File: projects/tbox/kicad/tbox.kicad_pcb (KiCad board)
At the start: 4 copper layers, 300 x 270 mm, 355 parts, among them J1001 PHONES A 3.5, J1002 PHONES A 1/4, J1003 PHONES B 3.5, J1004 PHONES B 1/4, J1005 TO CTRL J2001, J1101 MIC 3.5, J1102 MIC 1/4, J1103 HEADSET, J1104 SPARE, J1301 MIC 3.5, J1302 MIC 1/4, J1303 HEADSET, J1304 SPARE, J2001 TO FRONT J1005, J2002 TO REAR J3001, J3001 TO CTRL J2002, J3101 PWR IN (panel Powerpole), J3201 PTT A 3.5, J3202 PTT A 1/4, J3203 PTT B 3.5, J3204 PTT B 1/4, J3205 CW SPARE, J3206 RIG DE-9, J3301 LINE L SRC, J3302 LINE R SRC, J3303 LINE OUT, Q2101 2N7002, Q2102 2N7002, Q2103 2N7002, Q2104 2N7002, Q2105 2N7002, Q2106 2N7002, Q2107 2N7002, Q2201 MMBT3904, Q2202 2N7002, Q3201 2N7002, SW2101 PTT A, SW2102 PTT B, SW2103 OVERRIDE, SW2104 MUTE A, SW2105 MUTE B, SW2201 INTERCOM, SW3201 GAIN A HI, SW3202 GAIN B HI, SW3203 BIAS A, SW3204 BIAS B, T3301 600R:600R, T3302 600R:600R, U1101 OPA1678, U1102 TS12A12511, U1201 TS12A12511, U1301 OPA1678, U1302 TS12A12511, U1401 TS12A12511, U2201 OPA1678, U2301 TS12A12511, U2401 NJM4556A, U2402 OPA1678, U2403 NJM4556A, U3101 ADP7142AUJZ-5.0, U3102 OPA1678, U3103 TPS7A4701, U3301 OPA1678, U3302 OPA1678, U3401 OPA1678

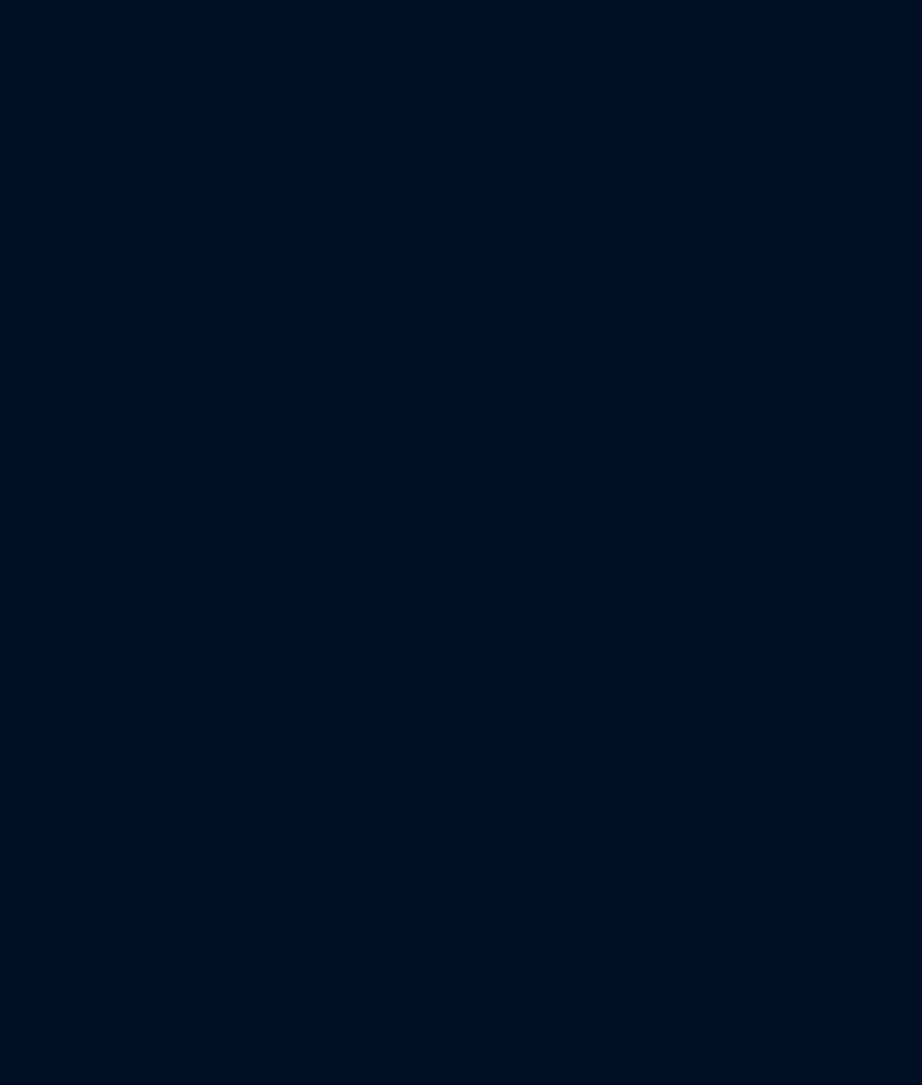
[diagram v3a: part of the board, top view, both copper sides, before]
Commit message: Footprints re-linked after the supply move (Update PCB from Schematic)
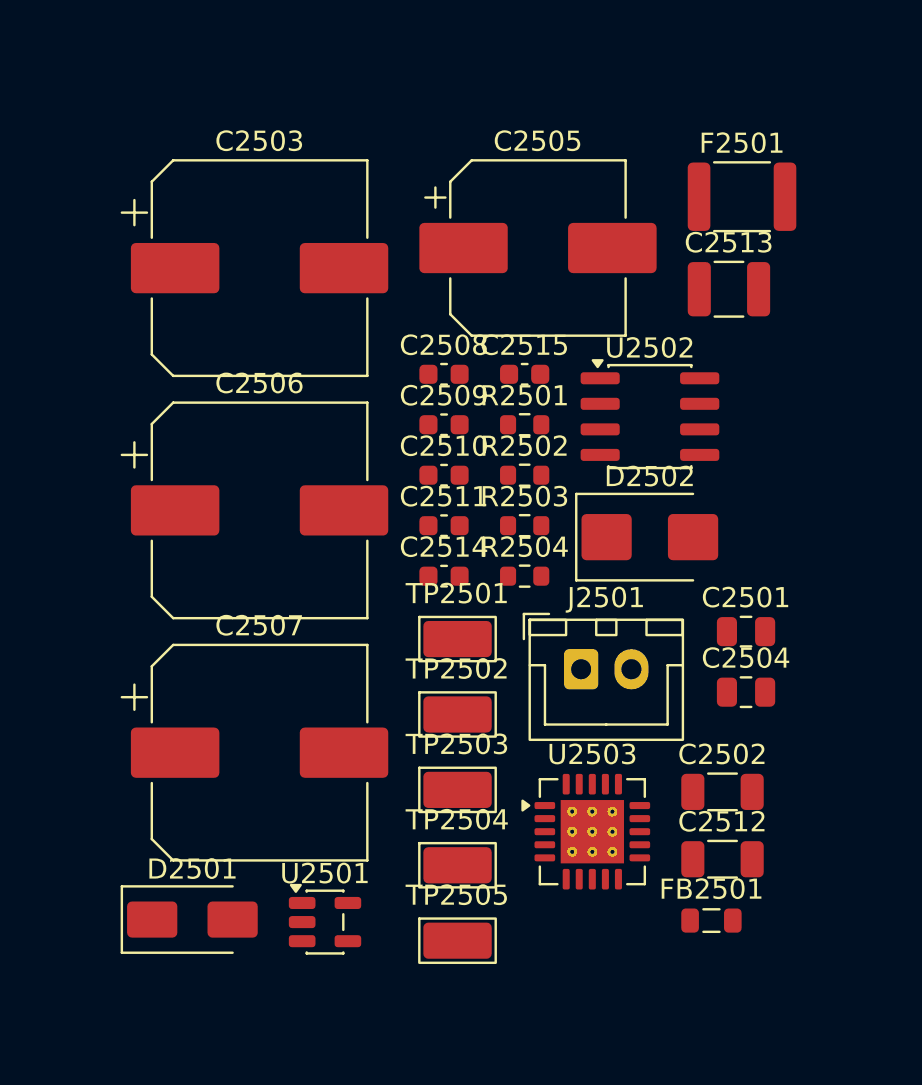
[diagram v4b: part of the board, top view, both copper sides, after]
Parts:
- added C2501: 4u7, Capacitor_SMD:C_0805_2012Metric, F.Cu at (94.6, 154.9)
- added C2502: 10u, Capacitor_SMD:C_1206_3216Metric, F.Cu at (93.4, 162.8)
- added C2503: 220u 35V, Capacitor_SMD:CP_Elec_10x10.5, F.Cu at (70.4, 136.8)
- added C2504: 4u7, Capacitor_SMD:C_0805_2012Metric, F.Cu at (94.6, 157.9)
- added C2505: 220u, Capacitor_SMD:CP_Elec_8x10.5, F.Cu at (84.3, 135.8)
- added C2506: 220u 35V, Capacitor_SMD:CP_Elec_10x10.5, F.Cu at (70.4, 148.8)
- added C2507: 470u, Capacitor_SMD:CP_Elec_10x10.5, F.Cu at (70.4, 160.9)
- added C2508: 100n, Capacitor_SMD:C_0603_1608Metric, F.Cu at (79.6, 142.1)
- added C2509: 100n, Capacitor_SMD:C_0603_1608Metric, F.Cu at (79.6, 144.6)
- added C2510: 1n, Capacitor_SMD:C_0603_1608Metric, F.Cu at (79.6, 147.1)
- added C2511: 100n, Capacitor_SMD:C_0603_1608Metric, F.Cu at (79.6, 149.6)
- added C2512: 10u, Capacitor_SMD:C_1206_3216Metric, F.Cu at (93.4, 166.2)
- added C2513: 47u X7R, Capacitor_SMD:C_1210_3225Metric, F.Cu at (93.8, 137.8)
- added C2514: 1u, Capacitor_SMD:C_0603_1608Metric, F.Cu at (79.6, 152.1)
- added C2515: 100n, Capacitor_SMD:C_0603_1608Metric, F.Cu at (83.6, 142.1)
- added D2501: SS34, Diode_SMD:D_SMA, F.Cu at (67.1, 169.2)
- added D2502: SMBJ18A, Diode_SMD:D_SMB, F.Cu at (89.8, 150.2)
- added F2501: PTC 500mA, Fuse:Fuse_1812_4532Metric, F.Cu at (94.4, 133.2)
- added FB2501: 600R, Inductor_SMD:L_0805_2012Metric, F.Cu at (92.9, 169.2)
- added J2501: PWR IN (panel Powerpole), Connector_JST:JST_XH_B2B-XH-A_1x02_P2.50mm_Vertical, F.Cu at (86.4, 156.7)
- added R2501: 10k, Resistor_SMD:R_0603_1608Metric, F.Cu at (83.6, 144.6)
- added R2502: 10k, Resistor_SMD:R_0603_1608Metric, F.Cu at (83.6, 147.1)
- added R2503: 47R, Resistor_SMD:R_0603_1608Metric, F.Cu at (83.6, 149.6)
- added R2504: 10R, Resistor_SMD:R_0603_1608Metric, F.Cu at (83.6, 152.1)
- added TP2501: TestPoint, TestPoint:TestPoint_Keystone_5015_Micro_Mini, F.Cu at (80.3, 155.2)
- added TP2502: TestPoint, TestPoint:TestPoint_Keystone_5015_Micro_Mini, F.Cu at (80.3, 159.0)
- added TP2503: TestPoint, TestPoint:TestPoint_Keystone_5015_Micro_Mini, F.Cu at (80.3, 162.7)
- added TP2504: TestPoint, TestPoint:TestPoint_Keystone_5015_Micro_Mini, F.Cu at (80.3, 166.5)
- added TP2505: TestPoint, TestPoint:TestPoint_Keystone_5015_Micro_Mini, F.Cu at (80.3, 170.2)
- added U2501: ADP7142AUJZ-5.0, Package_TO_SOT_SMD:TSOT-23-5, F.Cu at (73.7, 169.3)
- added U2502: OPA1678, Package_SO:SOIC-8_3.9x4.9mm_P1.27mm, F.Cu at (89.8, 144.2)
- added U2503: TPS7A4701, Package_DFN_QFN:Texas_RGW0020A_VQFN-20-1EP_5x5mm_P0.65mm_EP3.15x3.15mm_ThermalVias, F.Cu at (87.0, 164.8)
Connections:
- J2002 pad 2: RAW_13V8 -> BIAS_5V
- J3001 pad 2: RAW_13V8 -> BIAS_5V

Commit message: Initial placement: top-panel anchors and clustered free parts; TY-250P as a real 8-pin symbol
place_panel.py now also places the control board's pots, buttons,
override toggle and LEDs from panel-top.svg (x_pcb = 300 - x, y_pcb =
190 - y), lays the ribbon headers in gaps between those parts, and
clusters every remaining part by sub-sheet around a hand-chosen anchor
near the panel parts it serves, nearest-first by netlist distance, on a
0.5 mm occupancy grid.  DRC is clean apart from the ratsnest.

The transformer's 6-7 tie could not live in the footprint (KiCad DRC
treats copper between no-net pads as a short), so the Triad TY-250P is
now its own symbol (tbox:TY-250P, pins in Triad numbering, CT flagged
no-connect) and the tie is a schematic wire -- an ordinary net that
gets routed.  Footprint pads renumbered to match; the two board
footprints refreshed with nets from the netlist.
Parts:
- removed C3101, C3104: 4u7, Capacitor_SMD:C_0805_2012Metric
- removed C3102, C3112: 10u, Capacitor_SMD:C_1206_3216Metric
- removed C3103, C3106: 220u 35V, Capacitor_SMD:CP_Elec_10x10.5
- removed C3105: 220u, Capacitor_SMD:CP_Elec_8x10.5
- removed C3107: 470u, Capacitor_SMD:CP_Elec_10x10.5
- removed C3108, C3109, C3111, C3115: 100n, Capacitor_SMD:C_0603_1608Metric
- removed C3110: 1n, Capacitor_SMD:C_0603_1608Metric
- removed C3113: 47u X7R, Capacitor_SMD:C_1210_3225Metric
- removed C3114: 1u, Capacitor_SMD:C_0603_1608Metric
- removed D3101: SS34, Diode_SMD:D_SMA
- removed D3102: SMBJ18A, Diode_SMD:D_SMB
- removed F3101: PTC 500mA, Fuse:Fuse_1812_4532Metric
- removed FB3101: 600R, Inductor_SMD:L_0805_2012Metric
- removed J3101: PWR IN (panel Powerpole), Connector_JST:JST_XH_B2B-XH-A_1x02_P2.50mm_Vertical
- removed R3101, R3102: 10k, Resistor_SMD:R_0603_1608Metric
- removed R3103: 47R, Resistor_SMD:R_0603_1608Metric
- removed R3104: 10R, Resistor_SMD:R_0603_1608Metric
- removed TP3101, TP3102, TP3103, TP3104, TP3105: TestPoint, TestPoint:TestPoint_Keystone_5015_Micro_Mini
- removed U3101: ADP7142AUJZ-5.0, Package_TO_SOT_SMD:TSOT-23-5
- removed U3102: OPA1678, Package_SO:SOIC-8_3.9x4.9mm_P1.27mm
- removed U3103: TPS7A4701, Package_DFN_QFN:Texas_RGW0020A_VQFN-20-1EP_5x5mm_P0.65mm_EP3.15x3.15mm_ThermalVias
- T3301, T3302: value 600R:600R -> TY-250P
- moved SW2101 255.7 mm to (270.0, 58.5)
- moved U1301 240.4 mm to (39.7, 31.9)
- moved C1101 233.9 mm to (258.5, 35.8)
- moved R1307 232.0 mm to (32.5, 27.8)
- moved C1105 230.7 mm to (274.8, 30.6)
- moved R1306 228.0 mm to (32.5, 30.8)
- moved C1104 225.8 mm to (262.5, 35.8)
- moved R1305 224.1 mm to (32.5, 33.8)
- moved C1102 220.9 mm to (249.5, 35.8)
- moved R1303 212.2 mm to (36.5, 36.8)
- moved C1107 208.6 mm to (270.5, 35.8)
- moved R1308 208.2 mm to (60.5, 35.8)
- moved D2102 205.3 mm to (254.0, 59.0)
- moved C1103 202.9 mm to (235.5, 36.8)
- moved R2418 196.2 mm to (213.5, 106.8)
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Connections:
- T3301 pad 1: Net-(T3301-AA) -> (no net)
- T3301 pad 2: GND -> Net-(T3301-P1)
- T3301 pad 3: /Rear Board/Rig Out/LOUT_RET -> (no net)
- T3301 pad 4: Net-(T3301-SB) -> GND
- T3301 pad 5: (no net) -> Net-(T3301-S1)
- T3302 pad 1: Net-(T3302-AA) -> (no net)
- T3302 pad 2: GND -> Net-(T3302-P1)
- T3302 pad 3: /Rear Board/Rig Out/LOUT_RET -> (no net)
- T3302 pad 4: Net-(T3302-SB) -> GND
- T3302 pad 5: (no net) -> Net-(T3302-S1)

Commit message: Placement refinement: pull free parts toward their connections
After the cluster placement, --refine N passes (default 4) move each
free part toward the weighted centroid of the parts it shares signal
nets with, blended 15 % toward its sub-sheet anchor so sub-circuits
stay together; two-pin parts try both orientations; the occupancy grid
legalizes.  Ratsnest star length 13.8 m -> 9.4 m; DRC clean apart from
the ratsnest.  Free regions now exclude only the panel-edge strips.
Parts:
- moved R2120 158.5 mm to (32.8, 160.5), turned to 90 degrees
- moved FB3201 140.6 mm to (225.4, 167.3), turned to 90 degrees
- moved R3201 140.0 mm to (223.3, 154.0), turned to 90 degrees
- moved U2301 123.2 mm to (194.7, 155.3)
- moved R3209 116.8 mm to (216.5, 232.3)
- moved R2110 101.2 mm to (61.5, 61.3)
- moved R3203 101.1 mm to (189.0, 168.8)
- moved R2106 100.5 mm to (239.3, 61.0), turned to 90 degrees
- moved R3202 95.6 mm to (161.3, 153.5), turned to 90 degrees
- moved R2117 95.5 mm to (204.5, 146.8)
- moved R2101 88.7 mm to (198.3, 144.5), turned to 90 degrees
- moved FB2401 87.5 mm to (186.3, 35.4)
- moved FB2402 85.7 mm to (180.3, 35.4)
- moved R2102 85.7 mm to (150.0, 152.3)
- moved R2115 82.3 mm to (219.3, 61.0), turned to 90 degrees
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
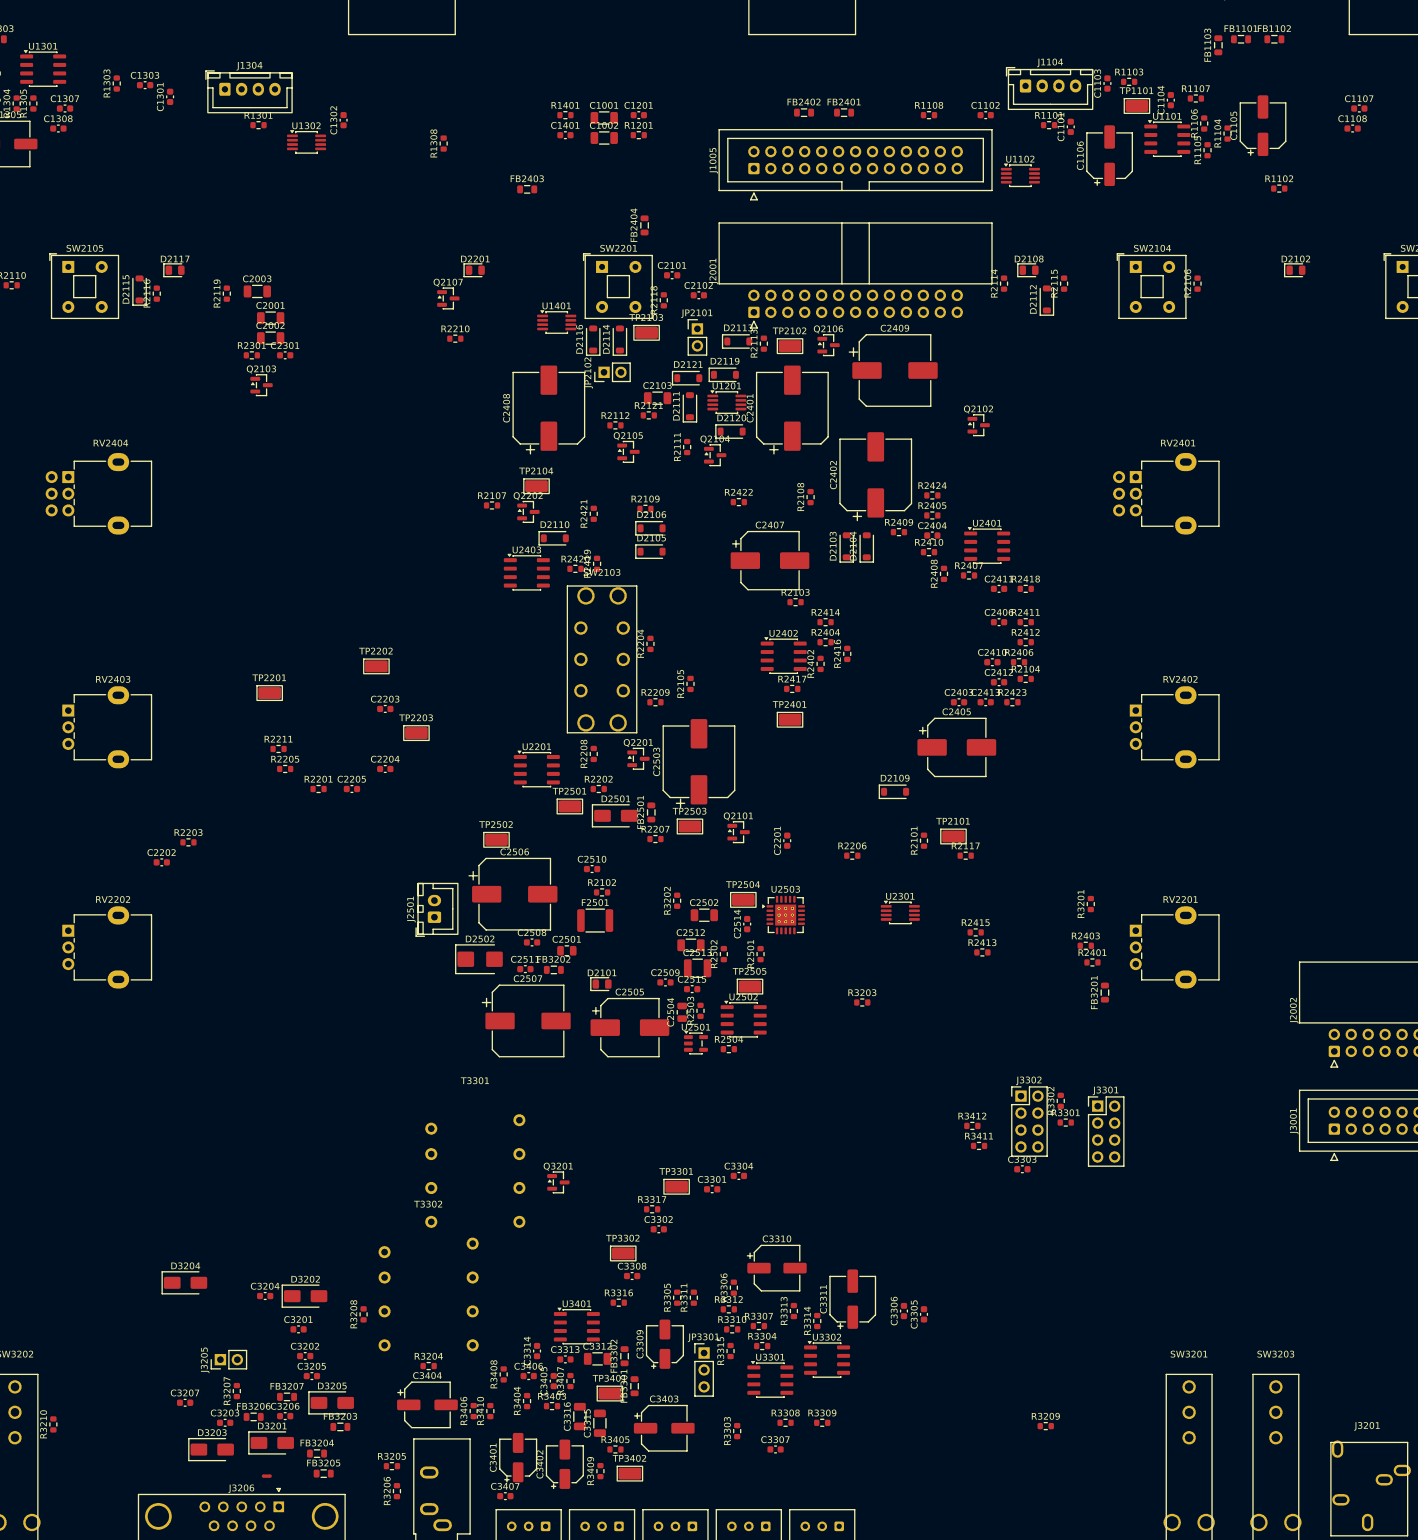
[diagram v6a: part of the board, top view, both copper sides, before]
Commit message: Decoupling pass: every 100n on its IC's V+ pin, bulk caps beside the hungriest ICs
tools/place_decoupling.py pairs each rail-to-GND cap with an IC on its own
sub-sheet (100n by schematic proximity, one per IC first; bulk by Load_mA),
then parks it against that pad -- long axis along the pin, rail pad toward
the IC -- evicting small passives from the slot when needed. All 100n now
sit within 4 mm of their pin; DRC unchanged apart from silk.
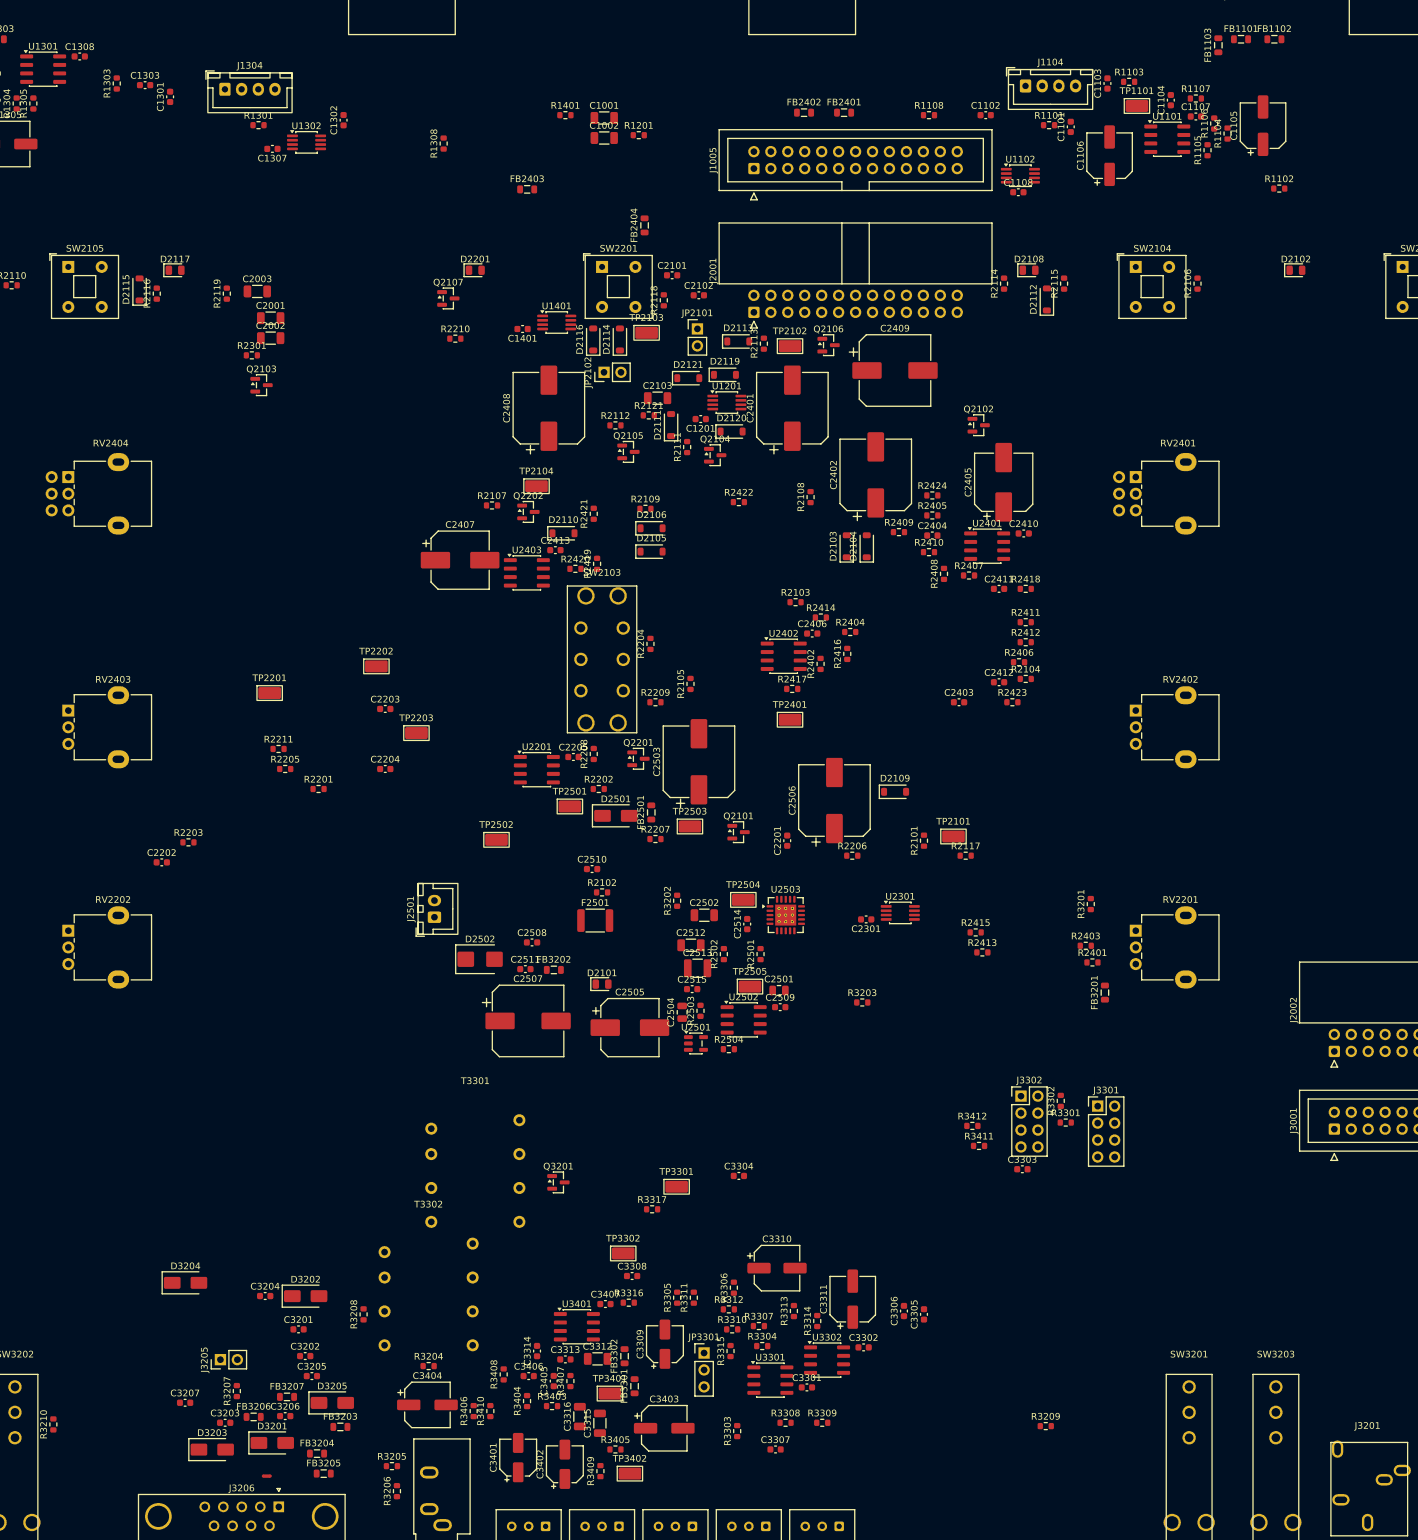
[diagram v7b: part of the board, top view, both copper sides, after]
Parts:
- moved C2301 121.4 mm to (189.6, 156.3), turned to 180 degrees
- moved C2413 68.4 mm to (143.0, 101.0)
- moved C1108 51.0 mm to (212.4, 47.3)
- moved C2506 49.9 mm to (184.8, 138.5), turned to 90 degrees
- moved C1201 46.5 mm to (164.8, 81.3), turned to 180 degrees
- moved C2407 46.5 mm to (128.7, 102.5)
- moved C2405 40.4 mm to (210.2, 90.8), turned to 90 degrees
- moved C3302 35.4 mm to (189.2, 220.5)
- moved C2205 33.5 mm to (145.7, 132.0)
- moved C3301 32.9 mm to (180.7, 226.5)
- moved C3407 32.5 mm to (150.5, 214.0)
- moved C2501 32.4 mm to (176.5, 167.0)
- moved C1307 31.7 mm to (100.6, 40.8), turned to 180 degrees
- moved C1401 29.8 mm to (138.1, 67.8), turned to 180 degrees
- moved C2406 28.1 mm to (181.5, 113.5)
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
